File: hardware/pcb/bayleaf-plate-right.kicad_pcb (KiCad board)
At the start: 2 copper layers, 137.3 x 94.7 mm, 7 parts

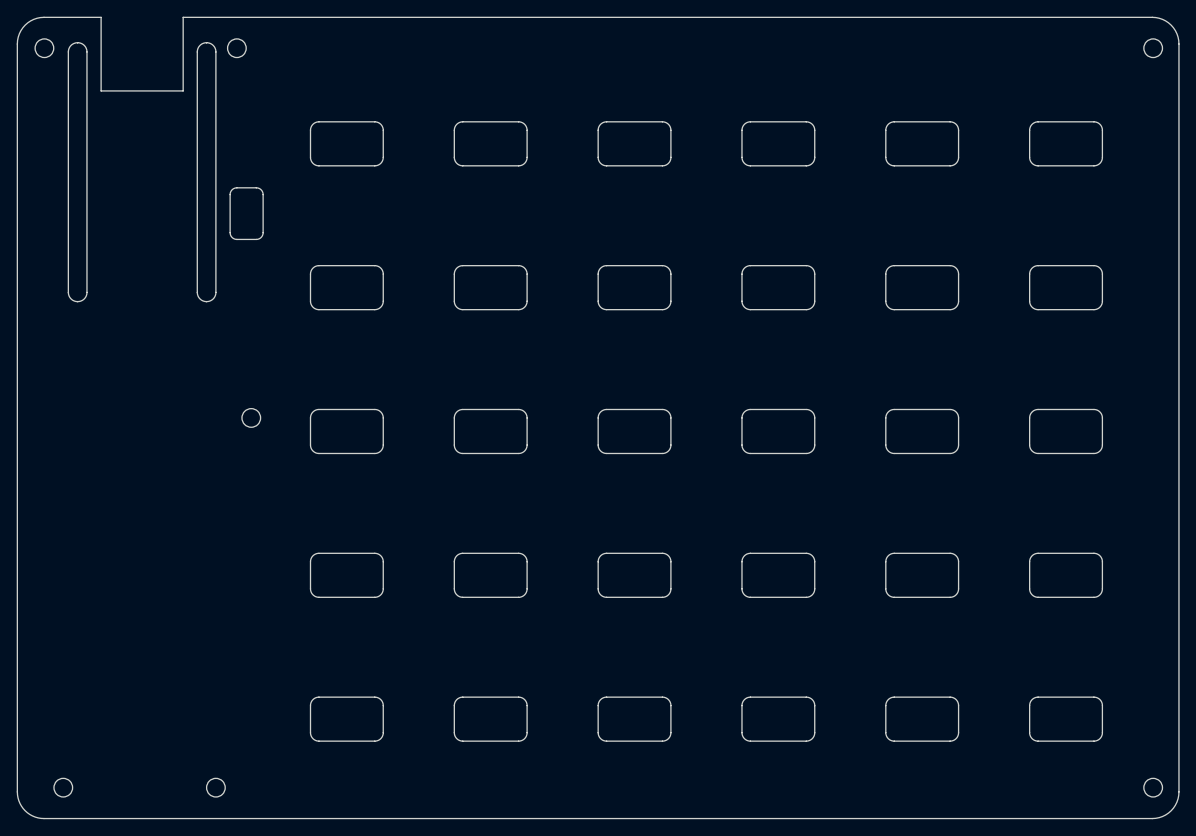
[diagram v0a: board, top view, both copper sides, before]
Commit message: Switch frame anchors solderable from below: plated holes in the anchor pads
- Kailh_PG1316S_castellated: each 2x2 mm frame-anchor pad gets a 0.7 mm plated hole with a
  1.4 mm pad on the bottom, so the whole switch can be soldered from the underside with an
  iron (hotplate still works). Switch window narrowed to 7.2 mm to keep routing channels.
- Bottom plates: 2.6 mm windows under every anchor hole; silkscreen moved under the battery.
- Router: plain notches again (the 0.3 mm margin choked Freerouting); every attempt is now
  rejected if it leaves copper on a window edge.
- Docs: iron-only switch procedure (untested, try one switch first), hotplate optional.

Co-Authored-By: Claude Opus 5.5 <noreply@anthropic.com>
Claude-Session: https://claude.ai/code/session_01C1HRLCKaYQawWFomwAvAgT
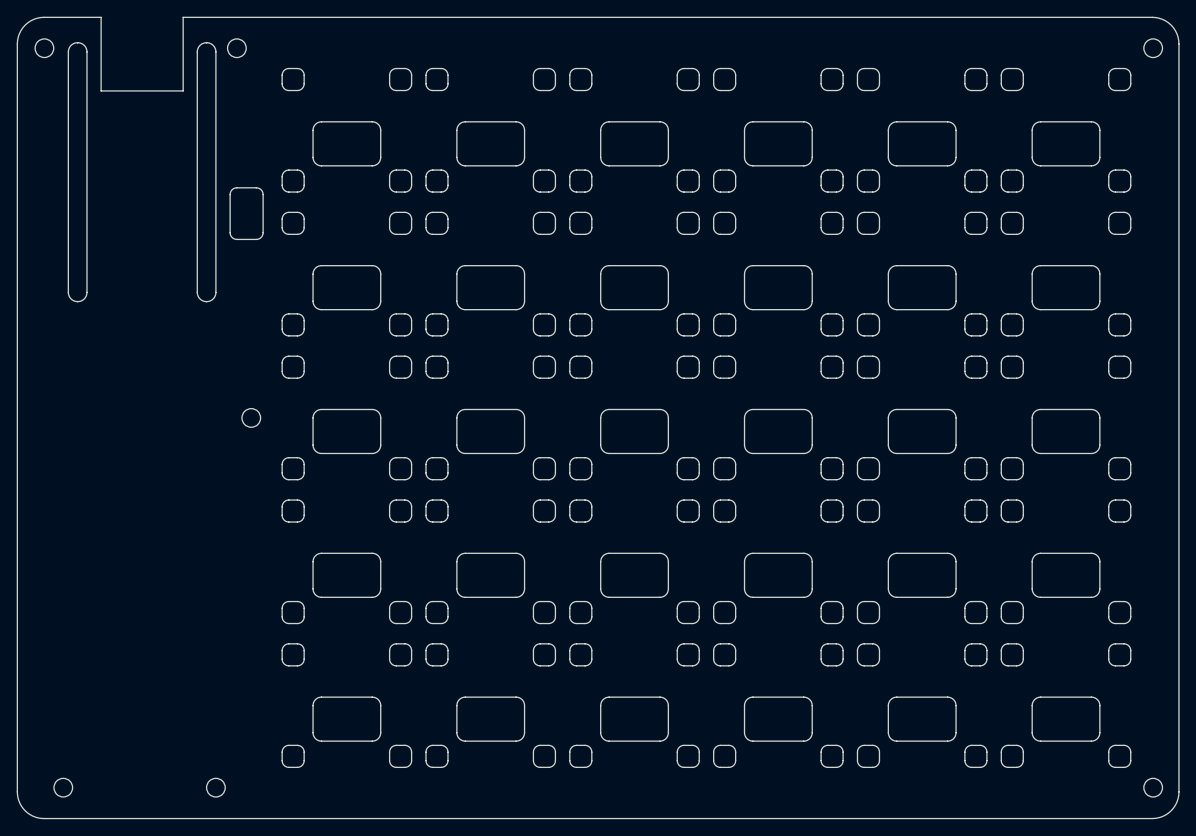
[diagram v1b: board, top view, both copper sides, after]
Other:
- outline, holes or cut-outs redrawn
- board text added: "right - FR4, no copper"
- board text removed: "right - FR4 bottom plate, no copper"
